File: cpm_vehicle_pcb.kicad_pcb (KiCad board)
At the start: 2 copper layers, 72 parts, among them IC1 ATMEGAAU, IC2 RPI-ZERO, J1 Conn_02x03_Counter_Clockwise, J2 Conn_02x03_Counter_Clockwise, J3 Conn_01x05, J4 USB4105-GF-A, J5 USB_B_Mini, J6 Conn_01x03_Socket, P1 NCP1117, Q11 BSS123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

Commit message: routing2_a
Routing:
- net +3V3: track 17.2 -> 67.6 mm, vias 0 -> 2
- net +5V: track 229.7 -> 242.4 mm, vias 5 -> 6
- net Net-(U4-EN): track 23.8 -> 31.3 mm
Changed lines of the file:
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@@
+	(segment
+		(start 130.0655 86.922)
+		(end 130.0655 88.4845)
+		(width 0.8)
+		(layer "F.Cu")
+		(net 10)
+	)
 	(segment
 		(start 130.0655 86.922)
@@
 		(end 145.2 60.231)
 		(width 0.3)
+		(layer "F.Cu")
+		(net 10)
+	)
+	(segment
+		(start 130.0655 88.4845)
+		(end 129.29 89.26)
+		(width 0.8)
 		(layer "F.Cu")
 		(net 10)
@@
 		(net 10)
 	)
+	(via
+		(at 129.29 89.26)
+		(size 0.8)
+		(drill 0.6)
+		(layers "F.Cu" "B.Cu")
+		(net 10)
+	)
 	(segment
 		(start 99.6375 86.26)
@@
 	)
 	(segment
+		(start 129.29 86.89)
+		(end 129.29 89.26)
+		(width 0.8)
+		(layer "B.Cu")
+		(net 10)
+	)
+	(segment
 		(start 137.8 67.95)
 		(end 142.18 63.57)
@@
 		(start 104.5625 91.185)
 		(end 111.9225 91.185)
+		(width 0.8)
+		(layer "B.Cu")
+		(net 10)
+	)
+	(segment
+		(start 123.915 81.515)
+		(end 129.29 86.89)
 		(width 0.8)
 		(layer "B.Cu")
@@
 	)
 	(segment
+		(start 168.83 50.35)
+		(end 168.83 54.5)
+		(width 0.8)
+		(layer "F.Cu")
+		(net 11)
+	)
+	(segment
+		(start 170.67 48.51)
+		(end 168.83 50.35)
+		(width 0.8)
+		(layer "F.Cu")
+		(net 11)
+	)
+	(segment
 		(start 175.97 57.25)
 		(end 172.39 57.25)
@@
 	)
 	(segment
+		(start 170.67 47.755)
+		(end 170.67 48.51)
+		(width 0.8)
+		(layer "F.Cu")
+		(net 11)
+	)
+	(segment
 		(start 180.44 79.54)
 		(end 180.44 80.79)
@@
 	)
 	(segment
+		(start 106.945 62.77)
+		(end 105.565 64.15)
+		(width 0.8)
+		(layer "F.Cu")
+		(net 125)
+	)
+	(segment
+		(start 128.16 68.7)
+		(end 127.16 67.7)
+		(width 0.6)
+		(layer "F.Cu")
+		(net 125)
+	)
+	(segment
+		(start 130.0694 68.7)
+		(end 128.16 68.7)
+		(width 0.6)
+		(layer "F.Cu")
+		(net 125)
+	)
+	(segment
 		(start 102.24 58.065)
 		(end 102.24 47.52)
@@
 	)
 	(segment
+		(start 105.565 64.15)
+		(end 104.35 64.15)
+		(width 0.8)
+		(layer "F.Cu")
+		(net 125)
+	)
+	(segment
 		(start 106.945 62.77)
 		(end 102.24 58.065)
@@
 		(net 125)
 	)
+	(via
+		(at 104.35 64.15)
+		(size 0.8)
+		(drill 0.6)
+		(layers "F.Cu" "B.Cu")
+		(net 125)
+	)
+	(via
+		(at 127.16 67.7)
+		(size 0.8)
+		(drill 0.6)
+		(layers "F.Cu" "B.Cu")
+		(net 125)
+	)
+	(segment
+		(start 130.52 56.42)
+		(end 130.946325 56.42)
+		(width 0.8)
+		(layer "B.Cu")
+		(net 125)
+	)
+	(segment
+		(start 106.63 64.15)
+		(end 114.39 56.39)
+		(width 0.8)
+		(layer "B.Cu")
+		(net 125)
+	)
+	(segment
+		(start 104.35 64.15)
+		(end 106.63 64.15)
+		(width 0.8)
+		(layer "B.Cu")
+		(net 125)
+	)
+	(segment
+		(start 130.49 56.39)
+		(end 130.52 56.42)
+		(width 0.8)
+		(layer "B.Cu")
+		(net 125)
+	)
+	(segment
+		(start 132.41 62.45)
+		(end 127.16 67.7)
+		(width 0.8)
+		(layer "B.Cu")
+		(net 125)
+	)
+	(segment
+		(start 132.41 57.883675)
+		(end 132.41 62.45)
+		(width 0.8)
+		(layer "B.Cu")
+		(net 125)
+	)
+	(segment
+		(start 130.946325 56.42)
+		(end 132.41 57.883675)
+		(width 0.8)
+		(layer "B.Cu")
+		(net 125)
+	)
+	(segment
+		(start 114.39 56.39)
+		(end 130.49 56.39)
+		(width 0.8)
+		(layer "B.Cu")
+		(net 125)
+	)

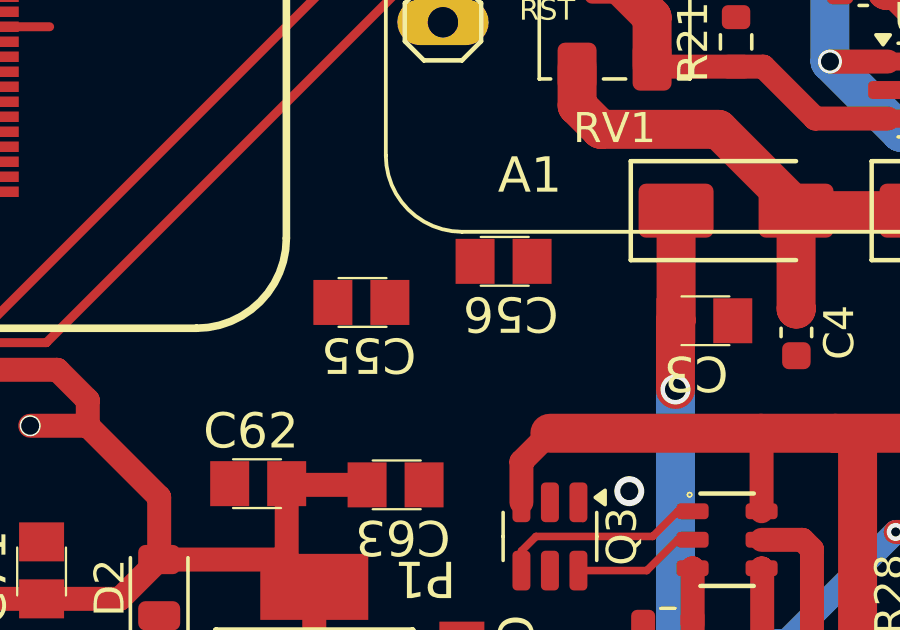
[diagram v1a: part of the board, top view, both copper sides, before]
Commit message: Added Bq25887
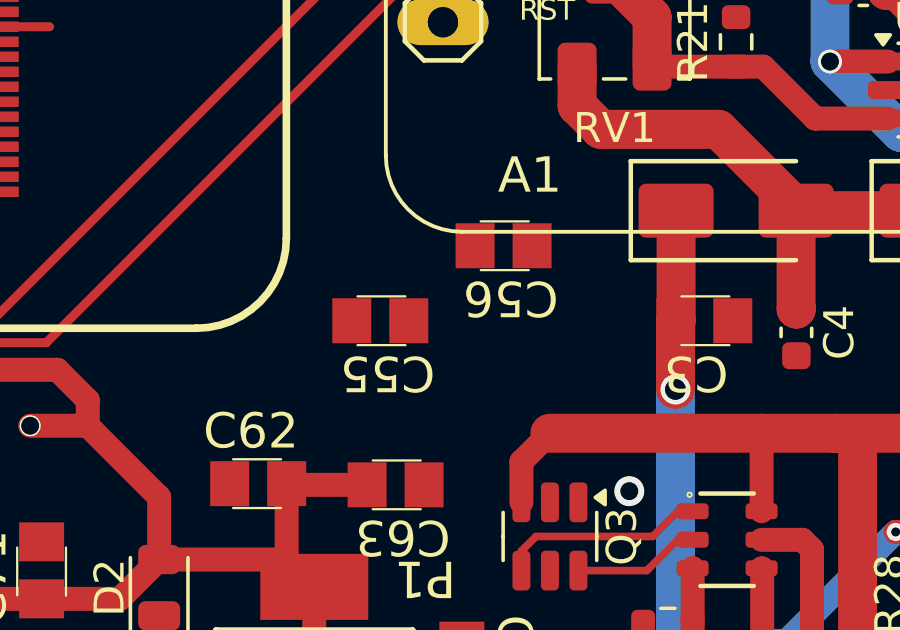
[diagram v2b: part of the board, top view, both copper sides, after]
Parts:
- moved C55 0.88 mm to (162.0, 72.5)
- moved C56 0.52 mm to (166.1, 70.0)
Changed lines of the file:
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@@
 	(footprint "footprints_vehicle_pcb:C0805_10681391"
 		(layer "F.Cu")
-		(at 161.37 71.89)
+		(at 162 72.5)
 		(descr "CAPACITOR")
 		(property "Reference" "C55"
@@
 	(footprint "footprints_vehicle_pcb:C0805_10681391"
 		(layer "F.Cu")
-		(at 166.11 70.52)
+		(at 166.11 70)
 		(descr "CAPACITOR")
 		(property "Reference" "C56"
@@
 		)
 		(property "Value" "330"
-			(at 0 1.43 90)
+			(at 0.125 1.07 90)
 			(layer "F.Fab")
 			(effects

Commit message: Schematic BQ25887
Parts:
- removed R51: 10k 0,1%, Resistor_SMD:R_0603_1608Metric
- removed R52: 1k 0,1%, Resistor_SMD:R_0603_1608Metric
- added C1: 10uF, Capacitor_THT:C_Disc_D5.0mm_W2.5mm_P2.50mm, F.Cu at (110.8, 98.8)
- added C12: 10uF, Capacitor_THT:C_Disc_D5.0mm_W2.5mm_P2.50mm, F.Cu at (110.8, 115.0)
- added C2: 44uF, Capacitor_THT:C_Disc_D5.0mm_W2.5mm_P2.50mm, F.Cu at (110.8, 102.8)
- added C5: 4.7uF, Capacitor_THT:C_Disc_D5.0mm_W2.5mm_P2.50mm, F.Cu at (110.8, 106.8)
- added C6: 1uF, footprints_vehicle_pcb:C0805_10681391, F.Cu at (111.0, 118.4)
- added C8: 47nF, Capacitor_THT:C_Disc_D5.0mm_W2.5mm_P2.50mm, F.Cu at (110.8, 110.9)
- added J7: USB4105-GF-A, footprints_vehicle_pcb:GCT_USB4105-GF-A, F.Cu at (124.9, 103.4)
- added L2: 1uH, Inductor_SMD:L_10.4x10.4_H4.8, F.Cu at (125.6, 112.8)
- added R19: 383, Resistor_SMD:R_0603_1608Metric, F.Cu at (117.3, 98.0)
- added R20: 2.2K, Resistor_SMD:R_0603_1608Metric, F.Cu at (117.3, 100.5)
- added R22: 300, Resistor_SMD:R_0603_1608Metric, F.Cu at (117.3, 103.0)
- added R23: 1k, Resistor_SMD:R_0603_1608Metric, F.Cu at (117.3, 105.5)
- added R29: 5.23K, Resistor_SMD:R_0603_1608Metric, F.Cu at (117.3, 108.0)
- added R30: 1k, Resistor_SMD:R_0603_1608Metric, F.Cu at (117.3, 110.5)
- added R31: 1k, Resistor_SMD:R_0603_1608Metric, F.Cu at (117.3, 113.0)
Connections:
- A1 pad 3: GND -> B-
- C10 pad 1: GND -> B-
- C3 pad 2: GND -> B-
- C31 pad 2: GND -> B-
- C4 pad 2: GND -> B-
- C41 pad 2: GND -> B-
- C42 pad 2: GND -> B-
- C51 pad 2: GND -> B-
- C53 pad 2: GND -> B-
- C54 pad 2: GND -> B-
- C55 pad 2: GND -> B-
- C56 pad 2: GND -> B-
- C61 pad 2: GND -> B-
- C62 pad 2: GND -> B-
- C63 pad 2: GND -> B-
- C7 pad 1: GND -> B-
- C71 pad 1: GND -> B-
- D3 pad 1: GND -> B-
- EXT_PINS0 pad 2: GND -> B-
- IC1 pad 11: GND -> B-
- IC1 pad 32: GND -> B-
- IC1 pad 62: GND -> B-
- IC1 pad 81: GND -> B-
- IC1 pad 88: Net-(IC1-PK1(ADC9/PCINT17)) -> unconnected-(IC1-PK1(ADC9/PCINT17)-Pad88)
- IC1 pad 99: GND -> B-
- IC2 pad 14: GND -> B-
- IC2 pad 20: GND -> B-
- IC2 pad 25: GND -> B-
- IC2 pad 30: GND -> B-
- IC2 pad 34: GND -> B-
- IC2 pad 39: GND -> B-
- IC2 pad 6: GND -> B-
- IC2 pad 9: GND -> B-
- J1 pad 6: GND -> B-
- J2 pad 5: GND -> B-
- J3 pad 3: GND -> B-
- J3 pad 4: GND -> B-
- J4 pad A1_B12: GND -> B-
- J4 pad B1_A12: GND -> B-
- J5 pad 5: GND -> B-
- J5 pad 6: GND -> B-
- P1 pad 1: GND -> B-
- Q11 pad 2: GND -> B-
- Q12 pad 2: GND -> B-
- Q13 pad 2: GND -> B-
- Q14 pad 2: GND -> B-
- Q3 pad 1: GND -> B-
- QG1 pad 2: GND -> B-
- QG2 pad 2: GND -> B-
- R/W0 pad 1: GND -> B-
- R21 pad 2: GND -> B-
- R24 pad 2: GND -> B-
- R9 pad 2: GND -> B-
- U3 pad 7: GND -> B-
- U4 pad 2: GND -> B-
- U7 pad 1: GND -> B-
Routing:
- net GND: track 13.3 -> 0.00 mm, vias 7 -> 0
- net B-: track 29.8 -> 43.1 mm, vias 0 -> 7
- added copper zone on B.Cu, net B-
- added copper zone on F.Cu, net B-
- removed copper zone on B.Cu, net GND
- removed copper zone on F.Cu, net GND

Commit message: v2
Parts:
- removed C3: 10uF, footprints_vehicle_pcb:C0805_10681391
- removed C4, C7: 22uF, Capacitor_SMD:C_0603_1608Metric
- removed D1, D6: SS54, PCM_JLCPCB:D_SMA
- removed J4: USB4105-GF-A, footprints_vehicle_pcb:GCT_USB4105-GF-A
- removed L1: 20uH, Inductor_SMD:L_10.4x10.4_H4.8
- removed R21: 3.3K, Resistor_SMD:R_0603_1608Metric
- removed RV1: R_Potentiometer, Potentiometer_SMD:Potentiometer_Bourns_3214W_Vertical
- removed U4: MT3608, Package_TO_SOT_SMD:SOT-23-6
- added U2: BQ25887RGET, BQ25887RGET:QFN50P400X400X100-25N, F.Cu at (168.2, 55.2)
- moved L2 75.7 mm to (177.1, 57.3), turned to -90 degrees
- moved J7 75.3 mm to (175.9, 48.0)
- moved A1 55.4 mm to (157.9, 109.5)
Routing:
- net Net-(U4-EN): track 31.3 -> 0.00 mm
- net Net-(U4-SW): track 30.0 -> 0.00 mm, vias 3 -> 0
- net /SDA: track 27.7 -> 6.44 mm
- net /SCL: track 29.5 -> 9.73 mm
- net Net-(C4-Pad1): track 17.4 -> 0.00 mm
- net Net-(U4-FB): track 12.0 -> 0.00 mm
- net +5V: track 242.4 -> 235.7 mm
- net +8.5V: track 18.7 -> 12.8 mm

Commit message: DONE
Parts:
- removed J7: USB4105-GF-A, footprints_vehicle_pcb:GCT_USB4105-GF-A
- added D4: LED, LED_SMD:LED_0805_2012Metric, F.Cu at (160.4, 48.2)
- added J4: USB3090-XX-X_REVE2, USB3090-XX-X_REVE2:GCT_USB3090-XX-X_REVE2, F.Cu at (167.4, 45.7)
- added R5: 1k, Resistor_SMD:R_0603_1608Metric, F.Cu at (167.9, 62.2)
- added R6: 1k, Resistor_SMD:R_0603_1608Metric, F.Cu at (169.5, 61.4)
- C1, C12, C2, C5, C8: footprint Capacitor_THT:C_Disc_D5.0mm_W2.5mm_P2.50mm -> footprints_vehicle_pcb:C0805_10681391
- moved C6 90.0 mm to (170.8, 51.1), turned to -90 degrees
- moved C8 85.6 mm to (179.6, 60.1), turned to 90 degrees
- moved C2 79.7 mm to (177.5, 59.2), turned to 90 degrees
- moved C1 78.1 mm to (173.3, 51.9), turned to -90 degrees
- moved C12 76.8 mm to (174.9, 72.7), turned to 90 degrees
- moved C5 72.7 mm to (172.3, 68.1), turned to -90 degrees
- moved R23 72.6 mm to (178.9, 67.1), turned to 90 degrees
- moved R22 69.9 mm to (177.3, 67.1), turned to 90 degrees
- moved R31 69.2 mm to (169.0, 67.2), turned to 180 degrees
- moved R29 68.6 mm to (170.7, 64.9), turned to 180 degrees
- moved R19 66.0 mm to (175.7, 67.1), turned to -90 degrees
- moved R30 65.9 mm to (169.0, 69.7)
- moved R20 64.8 mm to (160.4, 52.0), turned to 90 degrees
- moved A1 52.8 mm to (174.1, 59.2)
- moved C56 30.0 mm to (137.2, 62.0), turned to -90 degrees
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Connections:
- A1 pad 3: B- -> GND
- C1 pad 1: B- -> GND
- C10 pad 1: B- -> GND
- C12 pad 1: B+ -> +8.5V
- C12 pad 2: B- -> GND
- C2 pad 2: B- -> GND
- C31 pad 2: B- -> GND
- C41 pad 2: B- -> GND
- C42 pad 2: B- -> GND
- C5 pad 2: B- -> GND
- C51 pad 2: B- -> GND
- C53 pad 2: B- -> GND
- C54 pad 2: B- -> GND
- C55 pad 2: B- -> GND
- C56 pad 2: B- -> GND
- C6 pad 2: B- -> GND
- C61 pad 2: B- -> GND
- C62 pad 2: B- -> GND
- C63 pad 2: B- -> GND
- C71 pad 1: B- -> GND
- D3 pad 1: B- -> GND
- EXT_PINS0 pad 2: B- -> GND
- IC1 pad 11: B- -> GND
- IC1 pad 32: B- -> GND
- IC1 pad 62: B- -> GND
- IC1 pad 81: B- -> GND
- IC1 pad 99: B- -> GND
- IC2 pad 14: B- -> GND
- IC2 pad 20: B- -> GND
- IC2 pad 25: B- -> GND
- IC2 pad 3: unconnected-(IC2-GPIO2/SDA1-Pad3) -> SDA1
- IC2 pad 30: B- -> GND
- IC2 pad 34: B- -> GND
- IC2 pad 39: B- -> GND
- IC2 pad 5: unconnected-(IC2-GPIO3/SCL1-Pad5) -> SCL1
- IC2 pad 6: B- -> GND
- IC2 pad 9: B- -> GND
- J1 pad 6: B- -> GND
- J2 pad 5: B- -> GND
- J3 pad 3: B- -> GND
- J3 pad 4: B- -> GND
- J5 pad 5: B- -> GND
- J5 pad 6: B- -> GND
- P1 pad 1: B- -> GND
- Q11 pad 2: B- -> GND
- Q12 pad 2: B- -> GND
- Q13 pad 2: B- -> GND
- Q14 pad 2: B- -> GND
- Q3 pad 1: B- -> GND
- QG1 pad 2: B- -> GND
- QG2 pad 2: B- -> GND
- R/W0 pad 1: B- -> GND
- R19 pad 2: B- -> GND
- R20 pad 1: unconnected-(R20-Pad1) -> +5V
- R24 pad 2: B- -> GND
- R30 pad 1: B- -> GND
- R31 pad 2: B- -> GND
- R9 pad 2: B- -> GND
- U2 pad 13: B+ -> +8.5V
- U2 pad 14: B+ -> +8.5V
- U2 pad 19: B- -> GND
- U2 pad 20: B- -> GND
- U2 pad 4: unconnected-(U2-SDA-Pad4) -> /SDA
- U2 pad 5: unconnected-(U2-SCL-Pad5) -> /SCL
- U3 pad 7: B- -> GND
- U7 pad 1: B- -> GND
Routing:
- net /SDA: track 6.44 -> 35.8 mm
- net /SCL: track 9.73 -> 36.4 mm
- net +5V: track 235.7 -> 260.7 mm, vias 6 -> 5
- net GND: track 0.00 -> 22.8 mm, vias 0 -> 9
- net BB: track 2.96 -> 23.3 mm, vias 0 -> 1
- net Net-(D4-K): track 0.00 -> 20.2 mm
- net +8.5V: track 12.8 -> 32.1 mm, vias 1 -> 2
- net SW: track 0.00 -> 19.3 mm
- net VREGN: track 0.00 -> 18.9 mm
- net B-: track 43.1 -> 29.6 mm, vias 7 -> 0
- net PMID: track 0.00 -> 12.5 mm
- net Net-(J4-VBUS): track 0.00 -> 12.0 mm
- net Net-(U2-TS): track 0.00 -> 8.76 mm
- net Net-(U2-CBSET): track 0.00 -> 7.92 mm
- net Net-(U2-MID): track 0.00 -> 6.79 mm
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- added copper zone on B.Cu, net GND
- added copper zone on F.Cu, net GND
- removed copper zone on B.Cu, net B-
- removed copper zone on F.Cu, net B-
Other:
- board outline added: 95 x 50 mm

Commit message: some changes
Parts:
- added R7: 10k, Resistor_SMD:R_0603_1608Metric, F.Cu at (170.5, 55.5)
- SW1: value SW_DIP_x02 -> SW_DIP_x01
- SW2: value SW_SPDT_312 -> SW_SPST
- moved R20 6.51 mm to (160.7, 45.5), turned to -90 degrees
- moved D4 2.24 mm to (160.7, 50.4), turned to 90 degrees
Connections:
- C12 pad 1: +8.5V -> B+
- C41 pad 1: Net-(U3-VCCA) -> +3V3
- C42 pad 1: Net-(U3-VCCB) -> +5V
- C6 pad 1: Net-(J4-VBUS) -> VBUS
- J4 pad 1: Net-(J4-VBUS) -> VBUS
- R20 pad 1: +5V -> VBUS
- SW1 pad 1: Net-(U3-VCCA) -> Net-(U3-OE)
- SW1 pad 2: Net-(U3-VCCB) -> +3V3
- SW1 pad 3: +5V -> (no net)
- SW1 pad 4: +3V3 -> (no net)
- SW2 pad 3: +8.5V -> (no net)
- U2 pad 13: +8.5V -> B+
- U2 pad 14: +8.5V -> B+
- U2 pad 23: Net-(J4-VBUS) -> VBUS
- U2 pad 24: unconnected-(U2-PSEL-Pad24) -> Net-(U2-PSEL)
- U3 pad 1: Net-(U3-VCCA) -> +3V3
- U3 pad 14: Net-(U3-VCCB) -> +5V
- U3 pad 8: +3V3 -> Net-(U3-OE)
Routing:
- net +8.5V: track 32.1 -> 0.00 mm, vias 2 -> 0
- net B+: track 22.1 -> 54.2 mm, vias 0 -> 2
- net VBUS: track 0.00 -> 25.1 mm
- net Net-(U3-VCCB): track 16.4 -> 0.00 mm
- net (no net): track 0.00 -> 16.4 mm
- net +3V3: track 67.6 -> 81.5 mm
- net Net-(U3-VCCA): track 13.9 -> 0.00 mm
- net Net-(J4-VBUS): track 12.0 -> 0.00 mm
- net +5V: track 260.7 -> 269.6 mm, vias 5 -> 6
- net Net-(D4-K): track 20.2 -> 16.8 mm
- net Net-(U2-PSEL): track 0.00 -> 2.57 mm
- net Net-(Q3-S1/D2-Pad2): track 0.00 -> 2.28 mm, vias 0 -> 2
- net /R11: track 23.7 -> 21.9 mm
- net GND: track 22.8 -> 24.1 mm, vias 9 -> 10
- net Net-(D4-A): track 2.07 -> 3.13 mm
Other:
- board text added: "+5V"
- board text added: "GND"
